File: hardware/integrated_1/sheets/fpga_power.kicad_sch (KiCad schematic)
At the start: 8 parts, among them U1 XC6SLX9-TQG144, U2 MAX17620ATA

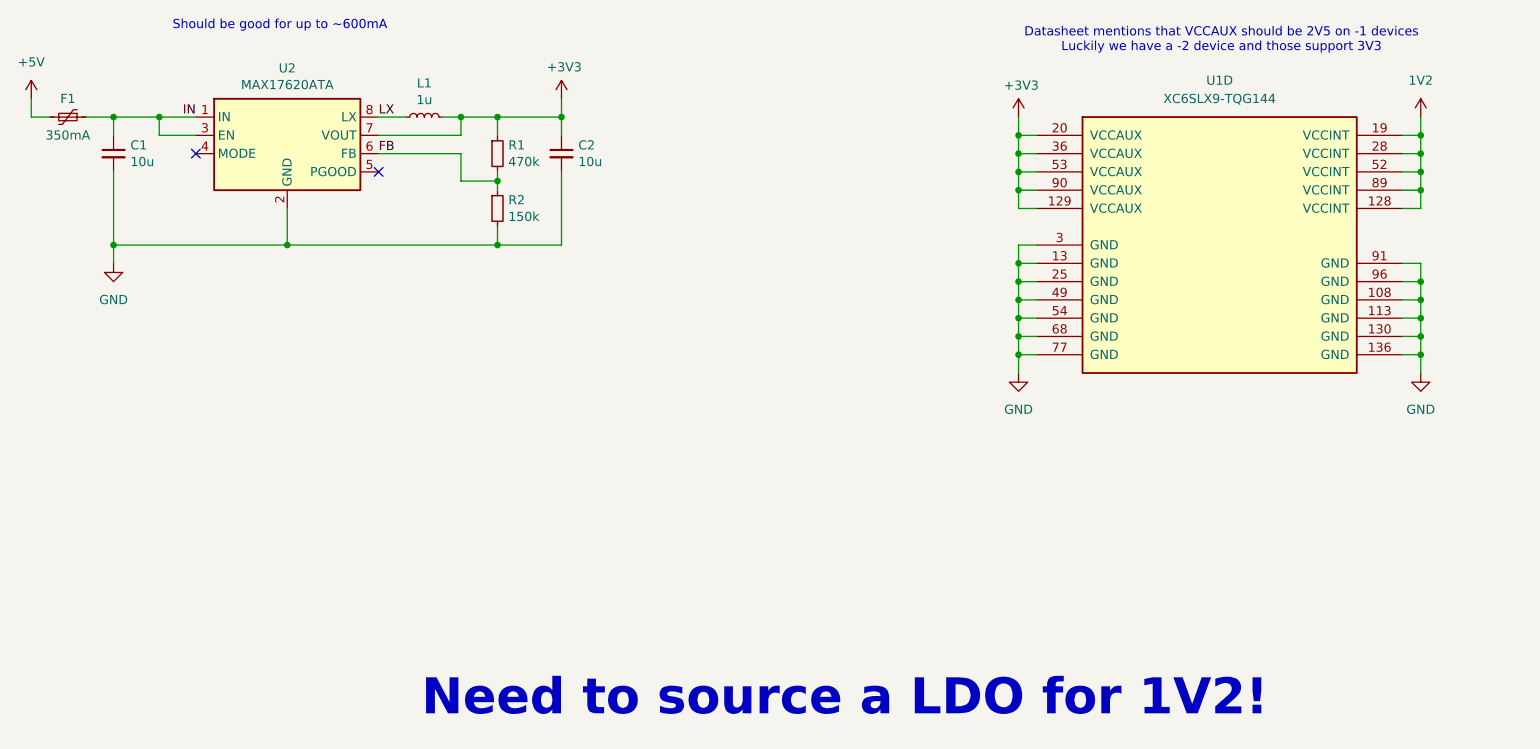
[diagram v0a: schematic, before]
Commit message: seperated converter from fpga power sheet
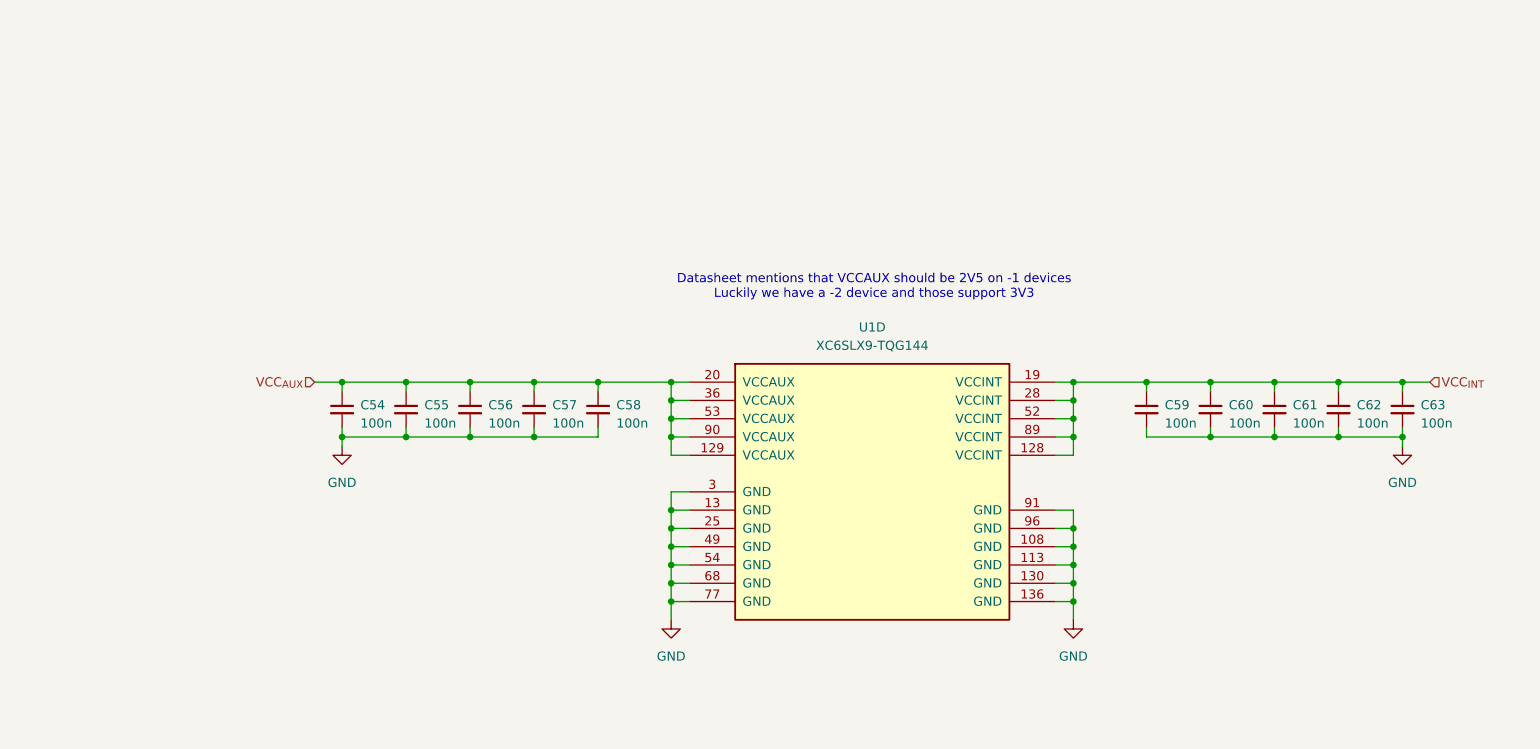
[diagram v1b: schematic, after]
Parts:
- removed C1, C2: 10u, Capacitor_SMD:C_0603_1608Metric, symbol Device:C_Small
- removed F1: 350mA, Fuse:Fuse_1206_3216Metric, symbol Device:Polyfuse_Small
- removed L1: 1u, Inductor_SMD:L_0603_1608Metric, symbol Device:L_Small
- removed R1: 470k, Resistor_SMD:R_0603_1608Metric, symbol Device:R_Small
- removed R2: 150k, Resistor_SMD:R_0603_1608Metric, symbol Device:R_Small
- removed U2: MAX17620ATA, Package_DFN_QFN:TDFN-8-1EP_2x2mm_P0.5mm_EP0.8x1.2mm, symbol Regulator_Switching:MAX17620ATA
- added C54, C55, C56, C57, C58, C59, C60, C61, C62, C63: 100n, Capacitor_SMD:C_0402_1005Metric, symbol Device:C_Small
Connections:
- net GND: now also C54.2, C55.2, C56.2, C57.2, C58.2, C59.2, C60.2, C61.2, C62.2, C63.2
- net +3V3 renamed VCC_{AUX}
- net VCC_{AUX}: now also C54.1, C55.1, C56.1, C57.1, C58.1
- net 1V2 renamed VCC_{INT}
- net VCC_{INT}: now also C59.1, C60.1, C61.1, C62.1, C63.1
- no-connect marks 2 -> 0
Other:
- note removed: "Need to source a LDO for 1V2!"
- note removed: "Should be good for up to ~600mA"
- title: FPGA Power Controllers and Connections -> FPGA Power
- moved on the sheet: U1D

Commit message: reannotated schematic
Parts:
- C1: renamed from C54; footprint Capacitor_SMD:C_0402_1005Metric -> KiCAD Library:C_0402_1005Metric
- C10: renamed from C63; footprint Capacitor_SMD:C_0402_1005Metric -> KiCAD Library:C_0402_1005Metric
- C2: renamed from C55; footprint Capacitor_SMD:C_0402_1005Metric -> KiCAD Library:C_0402_1005Metric
- C3: renamed from C56; footprint Capacitor_SMD:C_0402_1005Metric -> KiCAD Library:C_0402_1005Metric
- C4: renamed from C57; footprint Capacitor_SMD:C_0402_1005Metric -> KiCAD Library:C_0402_1005Metric
- C5: renamed from C58; footprint Capacitor_SMD:C_0402_1005Metric -> KiCAD Library:C_0402_1005Metric
- C6: renamed from C59; footprint Capacitor_SMD:C_0402_1005Metric -> KiCAD Library:C_0402_1005Metric
- C7: renamed from C60; footprint Capacitor_SMD:C_0402_1005Metric -> KiCAD Library:C_0402_1005Metric
- C8: renamed from C61; footprint Capacitor_SMD:C_0402_1005Metric -> KiCAD Library:C_0402_1005Metric
- C9: renamed from C62; footprint Capacitor_SMD:C_0402_1005Metric -> KiCAD Library:C_0402_1005Metric
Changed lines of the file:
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@@
 		(dnp no)
 		(fields_autoplaced yes)
-		(property "Reference" "C54"
+		(property "Reference" "C1"
 			(at 77.47 79.3813 0)
 			(effects
@@
 			)
 		)
-		(property "Footprint" "Capacitor_SMD:C_0402_1005Metric"
+		(property "Footprint" "KiCAD Library:C_0402_1005Metric"
 			(at 74.93 80.01 0)
 			(effects
@@
 			(project "integrated_1"
 				(path "/5cc60e42-d666-4a43-b4f0-3784ee4bf951/de200a54-0217-4ad2-b54c-599540b200bb"
-					(reference "C54")
+					(reference "C1")
 					(unit 1)
 				)
@@
 		(dnp no)
 		(fields_autoplaced yes)
-		(property "Reference" "C56"
+		(property "Reference" "C3"
 			(at 95.25 79.3813 0)
 			(effects
@@
 			)
 		)
-		(property "Footprint" "Capacitor_SMD:C_0402_1005Metric"
+		(property "Footprint" "KiCAD Library:C_0402_1005Metric"
 			(at 92.71 80.01 0)
 			(effects
@@
 			(project "integrated_1"
 				(path "/5cc60e42-d666-4a43-b4f0-3784ee4bf951/de200a54-0217-4ad2-b54c-599540b200bb"
-					(reference "C56")
+					(reference "C3")
 					(unit 1)
 				)
@@
 		(dnp no)
 		(fields_autoplaced yes)
-		(property "Reference" "C55"
+		(property "Reference" "C2"
 			(at 86.36 79.3813 0)
 			(effects
@@
 			)
 		)
-		(property "Footprint" "Capacitor_SMD:C_0402_1005Metric"
+		(property "Footprint" "KiCAD Library:C_0402_1005Metric"
 			(at 83.82 80.01 0)
 			(effects
@@
 			(project "integrated_1"
 				(path "/5cc60e42-d666-4a43-b4f0-3784ee4bf951/de200a54-0217-4ad2-b54c-599540b200bb"
-					(reference "C55")
+					(reference "C2")
 					(unit 1)
 				)
@@
 		(dnp no)
 		(fields_autoplaced yes)
-		(property "Reference" "C59"
+		(property "Reference" "C6"
 			(at 189.23 79.3813 0)
 			(effects
@@
 			)
 		)
-		(property "Footprint" "Capacitor_SMD:C_0402_1005Metric"
+		(property "Footprint" "KiCAD Library:C_0402_1005Metric"
 			(at 186.69 80.01 0)
 			(effects
@@
 			(project "integrated_1"
 				(path "/5cc60e42-d666-4a43-b4f0-3784ee4bf951/de200a54-0217-4ad2-b54c-599540b200bb"
-					(reference "C59")
+					(reference "C6")
 					(unit 1)
 				)
@@
 		(dnp no)
 		(fields_autoplaced yes)
-		(property "Reference" "C61"
+		(property "Reference" "C8"
 			(at 207.01 79.3813 0)
 			(effects
@@
 			)
 		)
-		(property "Footprint" "Capacitor_SMD:C_0402_1005Metric"
+		(property "Footprint" "KiCAD Library:C_0402_1005Metric"
 			(at 204.47 80.01 0)
 			(effects
@@
 			(project "integrated_1"
 				(path "/5cc60e42-d666-4a43-b4f0-3784ee4bf951/de200a54-0217-4ad2-b54c-599540b200bb"
-					(reference "C61")
+					(reference "C8")
 					(unit 1)
 				)
@@
 		(dnp no)
 		(fields_autoplaced yes)
-		(property "Reference" "#PWR058"
+		(property "Reference" "#PWR016"
 			(at 222.25 91.44 0)
 			(effects
@@
 			(project "integrated_1"
 				(path "/5cc60e42-d666-4a43-b4f0-3784ee4bf951/de200a54-0217-4ad2-b54c-599540b200bb"
-					(reference "#PWR058")
+					(reference "#PWR016")
 					(unit 1)
 				)
@@
 		(dnp no)
 		(fields_autoplaced yes)
-		(property "Reference" "C63"
+		(property "Reference" "C10"
 			(at 224.79 79.3813 0)
 			(effects
@@
 			)
 		)
-		(property "Footprint" "Capacitor_SMD:C_0402_1005Metric"
+		(property "Footprint" "KiCAD Library:C_0402_1005Metric"
 			(at 222.25 80.01 0)
 			(effects
@@
 			(project "integrated_1"
 				(path "/5cc60e42-d666-4a43-b4f0-3784ee4bf951/de200a54-0217-4ad2-b54c-599540b200bb"
-					(reference "C63")
+					(reference "C10")
 					(unit 1)
 				)
@@
 		(dnp no)
 		(fields_autoplaced yes)
-		(property "Reference" "C58"
+		(property "Reference" "C5"
 			(at 113.03 79.3813 0)
 			(effects
@@
 			)
 		)
-		(property "Footprint" "Capacitor_SMD:C_0402_1005Metric"
+		(property "Footprint" "KiCAD Library:C_0402_1005Metric"
 			(at 110.49 80.01 0)
 			(effects
@@
 			(project "integrated_1"
 				(path "/5cc60e42-d666-4a43-b4f0-3784ee4bf951/de200a54-0217-4ad2-b54c-599540b200bb"
-					(reference "C58")
+					(reference "C5")
 					(unit 1)
 				)
@@
 		(dnp no)
 		(fields_autoplaced yes)
-		(property "Reference" "#PWR057"
+		(property "Reference" "#PWR013"
 			(at 74.93 91.44 0)
 			(effects
@@
 			(project "integrated_1"
 				(path "/5cc60e42-d666-4a43-b4f0-3784ee4bf951/de200a54-0217-4ad2-b54c-599540b200bb"
-					(reference "#PWR057")
+					(reference "#PWR013")
 					(unit 1)
 				)
@@
 		(dnp no)
 		(fields_autoplaced yes)
-		(property "Reference" "#PWR020"
+		(property "Reference" "#PWR015"
 			(at 176.53 115.57 0)
 			(effects
@@
 			(project "integrated_1"
 				(path "/5cc60e42-d666-4a43-b4f0-3784ee4bf951/de200a54-0217-4ad2-b54c-599540b200bb"
-					(reference "#PWR020")
+					(reference "#PWR015")
 					(unit 1)
 				)
@@
 		(dnp no)
 		(fields_autoplaced yes)
-		(property "Reference" "C57"
+		(property "Reference" "C4"
 			(at 104.14 79.3813 0)
 			(effects
@@
 			)
 		)
-		(property "Footprint" "Capacitor_SMD:C_0402_1005Metric"
+		(property "Footprint" "KiCAD Library:C_0402_1005Metric"
 			(at 101.6 80.01 0)
 			(effects
@@
 			(project "integrated_1"
 				(path "/5cc60e42-d666-4a43-b4f0-3784ee4bf951/de200a54-0217-4ad2-b54c-599540b200bb"
-					(reference "C57")
+					(reference "C4")
 					(unit 1)
 				)
@@
 		(dnp no)
 		(fields_autoplaced yes)
-		(property "Reference" "C60"
+		(property "Reference" "C7"
 			(at 198.12 79.3813 0)
 			(effects
@@
 			)
 		)
-		(property "Footprint" "Capacitor_SMD:C_0402_1005Metric"
+		(property "Footprint" "KiCAD Library:C_0402_1005Metric"
 			(at 195.58 80.01 0)
 			(effects
@@
 			(project "integrated_1"
 				(path "/5cc60e42-d666-4a43-b4f0-3784ee4bf951/de200a54-0217-4ad2-b54c-599540b200bb"
-					(reference "C60")
+					(reference "C7")
 					(unit 1)
 				)
@@
 		(dnp no)
 		(fields_autoplaced yes)
-		(property "Reference" "#PWR019"
+		(property "Reference" "#PWR014"
 			(at 120.65 115.57 0)
 			(effects
@@
 			(project "integrated_1"
 				(path "/5cc60e42-d666-4a43-b4f0-3784ee4bf951/de200a54-0217-4ad2-b54c-599540b200bb"
-					(reference "#PWR019")
+					(reference "#PWR014")
 					(unit 1)
 				)
@@
 		(dnp no)
 		(fields_autoplaced yes)
-		(property "Reference" "C62"
+		(property "Reference" "C9"
 			(at 215.9 79.3813 0)
 			(effects
@@
 			)
 		)
-		(property "Footprint" "Capacitor_SMD:C_0402_1005Metric"
+		(property "Footprint" "KiCAD Library:C_0402_1005Metric"
 			(at 213.36 80.01 0)
 			(effects
@@
 			(project "integrated_1"
 				(path "/5cc60e42-d666-4a43-b4f0-3784ee4bf951/de200a54-0217-4ad2-b54c-599540b200bb"
-					(reference "C62")
-					(unit 1)
-				)
+					(reference "C9")
+					(unit 1)
+				)

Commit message: reannotated
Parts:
- renumbered C8 to C10, C9 to C11, C10 to C12, C1 to C3, C2 to C4, C3 to C5, C4 to C6, C5 to C7, C6 to C8, C7 to C9
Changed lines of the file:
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@@
 		(dnp no)
 		(fields_autoplaced yes)
-		(property "Reference" "C1"
+		(property "Reference" "C3"
 			(at 77.47 79.3813 0)
 			(effects
@@
 			(project "integrated_1"
 				(path "/5cc60e42-d666-4a43-b4f0-3784ee4bf951/de200a54-0217-4ad2-b54c-599540b200bb"
-					(reference "C1")
+					(reference "C3")
 					(unit 1)
 				)
@@
 		(dnp no)
 		(fields_autoplaced yes)
-		(property "Reference" "C3"
+		(property "Reference" "C5"
 			(at 95.25 79.3813 0)
 			(effects
@@
 			(project "integrated_1"
 				(path "/5cc60e42-d666-4a43-b4f0-3784ee4bf951/de200a54-0217-4ad2-b54c-599540b200bb"
-					(reference "C3")
+					(reference "C5")
 					(unit 1)
 				)
@@
 		(dnp no)
 		(fields_autoplaced yes)
-		(property "Reference" "C2"
+		(property "Reference" "C4"
 			(at 86.36 79.3813 0)
 			(effects
@@
 			(project "integrated_1"
 				(path "/5cc60e42-d666-4a43-b4f0-3784ee4bf951/de200a54-0217-4ad2-b54c-599540b200bb"
-					(reference "C2")
+					(reference "C4")
 					(unit 1)
 				)
@@
 		(dnp no)
 		(fields_autoplaced yes)
-		(property "Reference" "C6"
+		(property "Reference" "C8"
 			(at 189.23 79.3813 0)
 			(effects
@@
 			(project "integrated_1"
 				(path "/5cc60e42-d666-4a43-b4f0-3784ee4bf951/de200a54-0217-4ad2-b54c-599540b200bb"
-					(reference "C6")
+					(reference "C8")
 					(unit 1)
 				)
@@
 		(dnp no)
 		(fields_autoplaced yes)
-		(property "Reference" "C8"
+		(property "Reference" "C10"
 			(at 207.01 79.3813 0)
 			(effects
@@
 			(project "integrated_1"
 				(path "/5cc60e42-d666-4a43-b4f0-3784ee4bf951/de200a54-0217-4ad2-b54c-599540b200bb"
-					(reference "C8")
+					(reference "C10")
 					(unit 1)
 				)
@@
 		(dnp no)
 		(fields_autoplaced yes)
-		(property "Reference" "#PWR016"
+		(property "Reference" "#PWR015"
 			(at 222.25 91.44 0)
 			(effects
@@
 			(project "integrated_1"
 				(path "/5cc60e42-d666-4a43-b4f0-3784ee4bf951/de200a54-0217-4ad2-b54c-599540b200bb"
-					(reference "#PWR016")
+					(reference "#PWR015")
 					(unit 1)
 				)
@@
 		(dnp no)
 		(fields_autoplaced yes)
-		(property "Reference" "C10"
+		(property "Reference" "C12"
 			(at 224.79 79.3813 0)
 			(effects
@@
 			(project "integrated_1"
 				(path "/5cc60e42-d666-4a43-b4f0-3784ee4bf951/de200a54-0217-4ad2-b54c-599540b200bb"
-					(reference "C10")
+					(reference "C12")
 					(unit 1)
 				)
@@
 		(dnp no)
 		(fields_autoplaced yes)
-		(property "Reference" "C5"
+		(property "Reference" "C7"
 			(at 113.03 79.3813 0)
 			(effects
@@
 			(project "integrated_1"
 				(path "/5cc60e42-d666-4a43-b4f0-3784ee4bf951/de200a54-0217-4ad2-b54c-599540b200bb"
-					(reference "C5")
+					(reference "C7")
 					(unit 1)
 				)
@@
 		(dnp no)
 		(fields_autoplaced yes)
-		(property "Reference" "#PWR013"
+		(property "Reference" "#PWR012"
 			(at 74.93 91.44 0)
 			(effects
@@
 			(project "integrated_1"
 				(path "/5cc60e42-d666-4a43-b4f0-3784ee4bf951/de200a54-0217-4ad2-b54c-599540b200bb"
-					(reference "#PWR013")
+					(reference "#PWR012")
 					(unit 1)
 				)
@@
 		(dnp no)
 		(fields_autoplaced yes)
-		(property "Reference" "#PWR015"
+		(property "Reference" "#PWR014"
 			(at 176.53 115.57 0)
 			(effects
@@
 			(project "integrated_1"
 				(path "/5cc60e42-d666-4a43-b4f0-3784ee4bf951/de200a54-0217-4ad2-b54c-599540b200bb"
-					(reference "#PWR015")
+					(reference "#PWR014")
 					(unit 1)
 				)
@@
 		(dnp no)
 		(fields_autoplaced yes)
-		(property "Reference" "C4"
+		(property "Reference" "C6"
 			(at 104.14 79.3813 0)
 			(effects
@@
 			(project "integrated_1"
 				(path "/5cc60e42-d666-4a43-b4f0-3784ee4bf951/de200a54-0217-4ad2-b54c-599540b200bb"
-					(reference "C4")
+					(reference "C6")
 					(unit 1)
 				)
@@
 		(dnp no)
 		(fields_autoplaced yes)
-		(property "Reference" "C7"
+		(property "Reference" "C9"
 			(at 198.12 79.3813 0)
 			(effects
@@
 			(project "integrated_1"
 				(path "/5cc60e42-d666-4a43-b4f0-3784ee4bf951/de200a54-0217-4ad2-b54c-599540b200bb"
-					(reference "C7")
+					(reference "C9")
 					(unit 1)
 				)
@@
 		(dnp no)
 		(fields_autoplaced yes)
-		(property "Reference" "#PWR014"
+		(property "Reference" "#PWR013"
 			(at 120.65 115.57 0)
 			(effects
@@
 			(project "integrated_1"
 				(path "/5cc60e42-d666-4a43-b4f0-3784ee4bf951/de200a54-0217-4ad2-b54c-599540b200bb"
-					(reference "#PWR014")
+					(reference "#PWR013")
 					(unit 1)
 				)
@@
 		(dnp no)
 		(fields_autoplaced yes)
-		(property "Reference" "C9"
+		(property "Reference" "C11"
 			(at 215.9 79.3813 0)
 			(effects
@@
 			(project "integrated_1"
 				(path "/5cc60e42-d666-4a43-b4f0-3784ee4bf951/de200a54-0217-4ad2-b54c-599540b200bb"
-					(reference "C9")
-					(unit 1)
-				)
+					(reference "C11")
+					(unit 1)
+				)
